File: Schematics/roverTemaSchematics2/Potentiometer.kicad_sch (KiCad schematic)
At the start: 3 parts, among them U1 ProS3

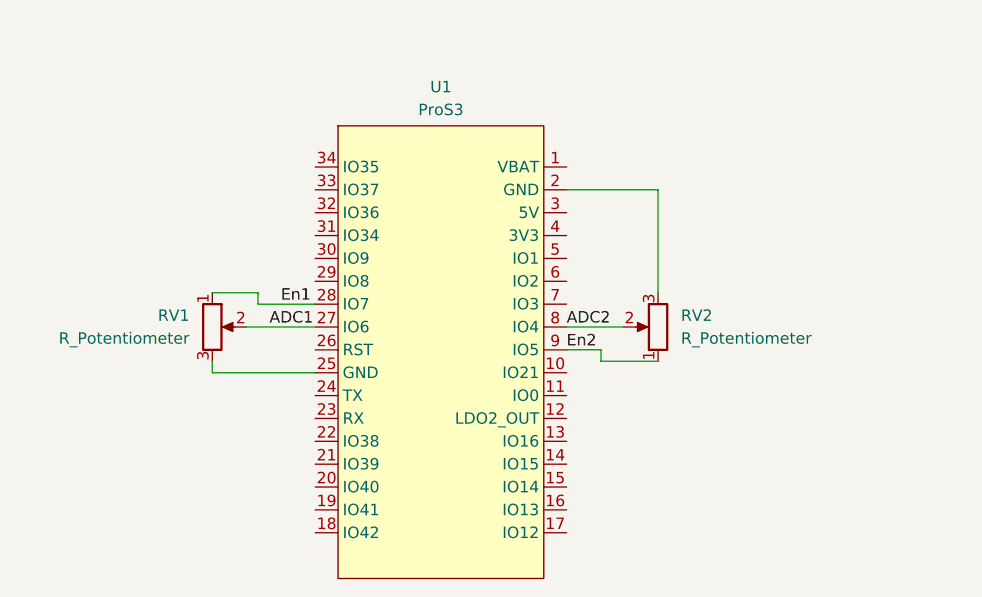
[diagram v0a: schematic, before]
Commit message: added button
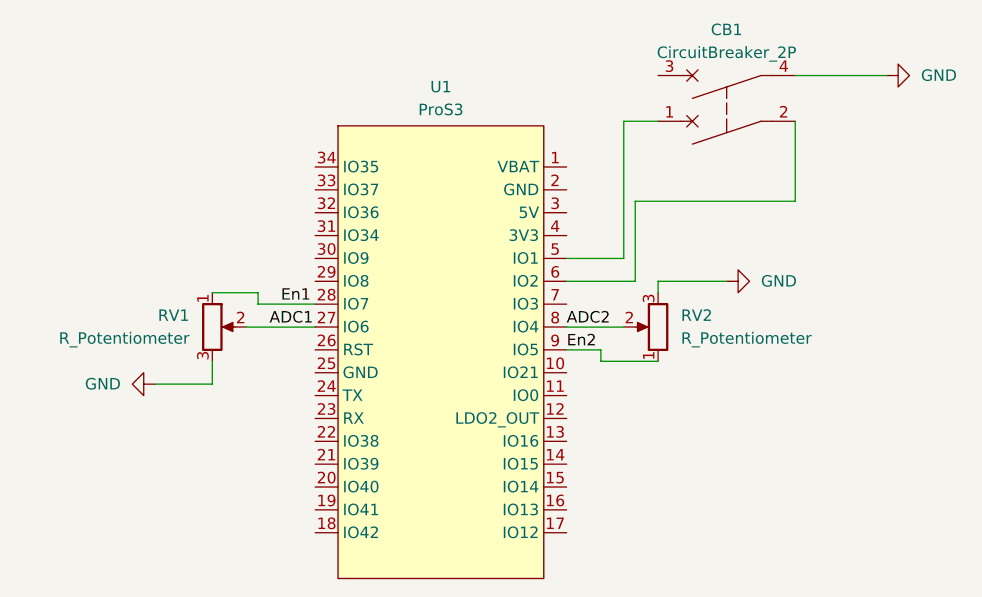
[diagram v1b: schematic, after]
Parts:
- added CB1: CircuitBreaker_2P, symbol Device:CircuitBreaker_2P
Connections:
- net at U1.2 (GND): no longer RV2.3
- net at U1.25 (GND): no longer RV1.3
- net at U1.5 (IO1): now also CB1.1
- net at U1.6 (IO2): now also CB1.2
- new net GND: CB1.4, RV1.3, RV2.3
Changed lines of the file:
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@@
 (kicad_sch (version 20230121) (generator eeschema)
   (paper "A4")
+  (wire (pts (xy 137.16 80.01) (xy 129.54 80.01))
+    (stroke (width 0) (type default))
+  )
   (wire (pts (xy 139.7 88.9) (xy 133.35 88.9))
     (stroke (width 0) (type default))
   )
-  (wire (pts (xy 139.7 69.85) (xy 129.54 69.85))
+  (wire (pts (xy 154.94 71.12) (xy 137.16 71.12))
+    (stroke (width 0) (type default))
+  )
+  (wire (pts (xy 135.89 77.47) (xy 135.89 62.23))
+    (stroke (width 0) (type default))
+  )
+  (wire (pts (xy 154.94 62.23) (xy 154.94 71.12))
+    (stroke (width 0) (type default))
+  )
+  (wire (pts (xy 137.16 71.12) (xy 137.16 80.01))
     (stroke (width 0) (type default))
   )
@@
     (stroke (width 0) (type default))
   )
-  (wire (pts (xy 139.7 81.28) (xy 139.7 69.85))
+  (wire (pts (xy 154.94 57.15) (xy 165.1 57.15))
     (stroke (width 0) (type default))
   )
@@
     (stroke (width 0) (type default))
   )
-  (wire (pts (xy 90.17 90.17) (xy 101.6 90.17))
+  (wire (pts (xy 129.54 77.47) (xy 135.89 77.47))
     (stroke (width 0) (type default))
   )
@@
     (stroke (width 0) (type default))
   )
+  (wire (pts (xy 90.17 91.44) (xy 83.82 91.44))
+    (stroke (width 0) (type default))
+  )
   (wire (pts (xy 95.25 81.28) (xy 95.25 82.55))
     (stroke (width 0) (type default))
@@
     (stroke (width 0) (type default))
   )
-  (wire (pts (xy 90.17 88.9) (xy 90.17 90.17))
+  (wire (pts (xy 135.89 62.23) (xy 139.7 62.23))
+    (stroke (width 0) (type default))
+  )
+  (wire (pts (xy 90.17 88.9) (xy 90.17 91.44))
+    (stroke (width 0) (type default))
+  )
+  (wire (pts (xy 139.7 80.01) (xy 147.32 80.01))
+    (stroke (width 0) (type default))
+  )
+  (wire (pts (xy 139.7 81.28) (xy 139.7 80.01))
     (stroke (width 0) (type default))
   )
@@
     )
   )
+  (symbol (lib_id "power:GND") (at 147.32 80.01 90) (unit 1)
+    (in_bom yes) (on_board yes) (dnp no) (fields_autoplaced)
+    (property "Reference" "#PWR01" (at 153.67 80.01 0)
+      (effects (font (size 1.27 1.27)) hide)
+    )
+    (property "Value" "GND" (at 151.13 80.01 90)
+      (effects (font (size 1.27 1.27)) (justify right))
+    )
+    (property "Footprint" "" (at 147.32 80.01 0)
+      (effects (font (size 1.27 1.27)) hide)
+    )
+    (property "Datasheet" "" (at 147.32 80.01 0)
+      (effects (font (size 1.27 1.27)) hide)
+    )
+    (pin "1")
+    (instances
+      (project "Potentiometer"
+        (path "/8419caec-7e83-40e4-9271-fff4c79099b1"
+          (reference "#PWR01") (unit 1)
+        )
+      )
+    )
+  )
   (symbol (lib_id "Device:R_Potentiometer") (at 90.17 85.09 0) (unit 1)
     (in_bom yes) (on_board yes) (dnp no) (fields_autoplaced)
@@
         (path "/8419caec-7e83-40e4-9271-fff4c79099b1"
           (reference "RV1") (unit 1)
+        )
+      )
+    )
+  )
+  (symbol (lib_id "power:GND") (at 165.1 57.15 90) (unit 1)
+    (in_bom yes) (on_board yes) (dnp no) (fields_autoplaced)
+    (property "Reference" "#PWR02" (at 171.45 57.15 0)
+      (effects (font (size 1.27 1.27)) hide)
+    )
+    (property "Value" "GND" (at 168.91 57.15 90)
+      (effects (font (size 1.27 1.27)) (justify right))
+    )
+    (property "Footprint" "" (at 165.1 57.15 0)
+      (effects (font (size 1.27 1.27)) hide)
+    )
+    (property "Datasheet" "" (at 165.1 57.15 0)
+      (effects (font (size 1.27 1.27)) hide)
+    )
+    (pin "1")
+    (instances
+      (project "Potentiometer"
+        (path "/8419caec-7e83-40e4-9271-fff4c79099b1"
+          (reference "#PWR02") (unit 1)
         )
       )
@@
         )
       )
+    )
+  )
+  (symbol (lib_id "power:GND") (at 83.82 91.44 270) (unit 1)
+    (in_bom yes) (on_board yes) (dnp no) (fields_autoplaced)
+    (property "Reference" "#PWR03" (at 77.47 91.44 0)
+      (effects (font (size 1.27 1.27)) hide)
+    )
+    (property "Value" "GND" (at 80.01 91.44 90)
+      (effects (font (size 1.27 1.27)) (justify right))
+    )
+    (property "Footprint" "" (at 83.82 91.44 0)
+      (effects (font (size 1.27 1.27)) hide)
+    )
+    (property "Datasheet" "" (at 83.82 91.44 0)
+      (effects (font (size 1.27 1.27)) hide)
+    )
+    (pin "1")
+    (instances
+      (project "Potentiometer"
+        (path "/8419caec-7e83-40e4-9271-fff4c79099b1"
+          (reference "#PWR03") (unit 1)
+        )
+      )
+    )
+  )
+  (symbol (lib_id "Device:CircuitBreaker_2P") (at 147.32 59.69 90) (unit 1)
+    (in_bom yes) (on_board yes) (dnp no) (fields_autoplaced)
+    (property "Reference" "CB1" (at 147.32 52.07 90)
+      (effects (font (size 1.27 1.27)))
+    )
+    (property "Value" "CircuitBreaker_2P" (at 147.32 54.61 90)
+      (effects (font (size 1.27 1.27)))
+    )
+    (property "Footprint" "" (at 147.32 62.23 0)
+      (effects (font (size 1.27 1.27)) hide)
+    )
+    (property "Datasheet" "~" (at 147.32 62.23 0)
+      (effects (font (size 1.27 1.27)) hide)
+    )
+    (pin "4")
+    (pin "1")
+    (pin "3")
+    (pin "2")
+    (instances
+      (project "Potentiometer"
+        (path "/8419caec-7e83-40e4-9271-fff4c79099b1"
+          (reference "CB1") (unit 1)
+        )
+      )
